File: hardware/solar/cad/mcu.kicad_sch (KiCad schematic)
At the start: 0 parts

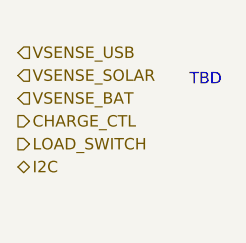
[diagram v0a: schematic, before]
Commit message: Add NTC circuit
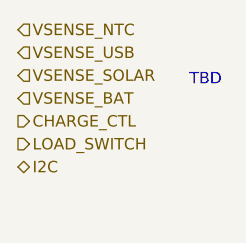
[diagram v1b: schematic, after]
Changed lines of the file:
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@@
+    (effects (font (size 1.27 1.27)) (justify left))
+  )
+  (hierarchical_label "VSENSE_NTC" (shape input) (at 96.52 80.01 0)
     (effects (font (size 1.27 1.27)) (justify left))
   )

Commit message: Add 200 mA (0.1C) trickle charger, neaten up schematic
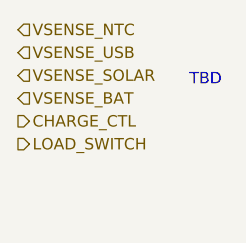
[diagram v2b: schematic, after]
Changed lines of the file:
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@@
-    (effects (font (size 1.27 1.27)) (justify left))
-  )
-  (hierarchical_label "I2C" (shape bidirectional) (at 96.52 95.25 0)
     (effects (font (size 1.27 1.27)) (justify left))
   )

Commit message: Add external I2C connection, LED resistors, op-amp power connections
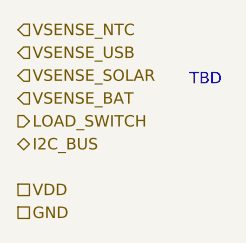
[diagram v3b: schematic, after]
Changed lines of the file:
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@@
     (effects (font (size 1.27 1.27)) (justify left bottom))
   )
-  (hierarchical_label "CHARGE_CTL" (shape output) (at 96.52 90.17 0)
+  (hierarchical_label "GND" (shape passive) (at 96.52 100.33 0)
+    (effects (font (size 1.27 1.27)) (justify left))
+  )
+  (hierarchical_label "I2C_BUS" (shape bidirectional) (at 96.52 92.71 0)
     (effects (font (size 1.27 1.27)) (justify left))
   )
@@
     (effects (font (size 1.27 1.27)) (justify left))
   )
-  (hierarchical_label "LOAD_SWITCH" (shape output) (at 96.52 92.71 0)
+  (hierarchical_label "LOAD_SWITCH" (shape output) (at 96.52 90.17 0)
     (effects (font (size 1.27 1.27)) (justify left))
   )
@@
     (effects (font (size 1.27 1.27)) (justify left))
   )
+  (hierarchical_label "VDD" (shape passive) (at 96.52 97.79 0)
+    (effects (font (size 1.27 1.27)) (justify left))
+  )
